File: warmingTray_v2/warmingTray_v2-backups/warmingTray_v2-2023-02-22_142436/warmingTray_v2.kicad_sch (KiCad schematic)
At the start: 37 parts, among them J1 Jack-DC, P1 Power, P2 Analog, P3 Analog, P4 Digital, P5 PWM, P6 PWM, P7 Communication

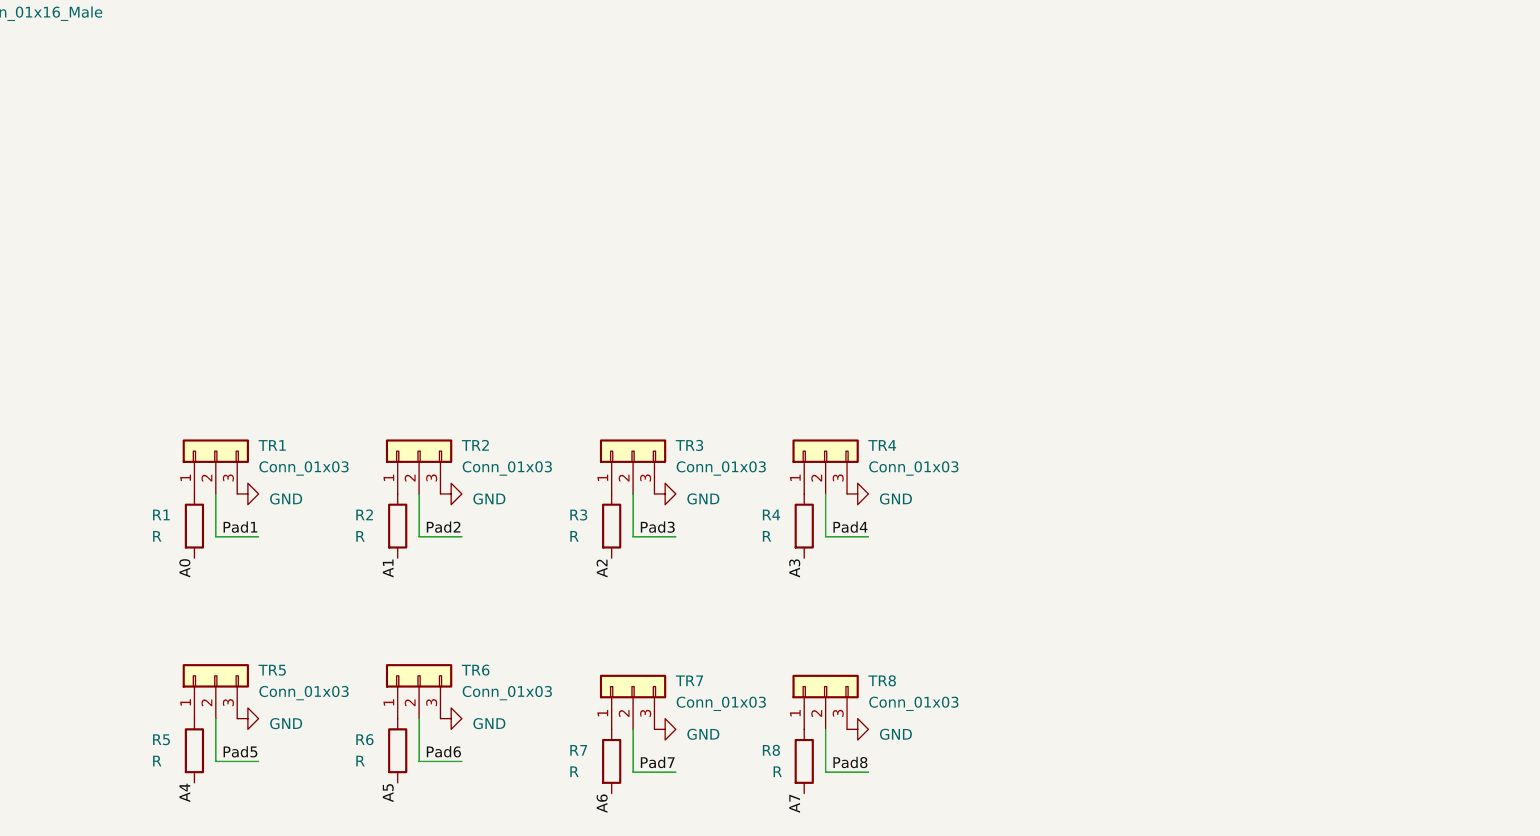
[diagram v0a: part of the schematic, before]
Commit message: Added footprints for transistor pins and surface mount resistors
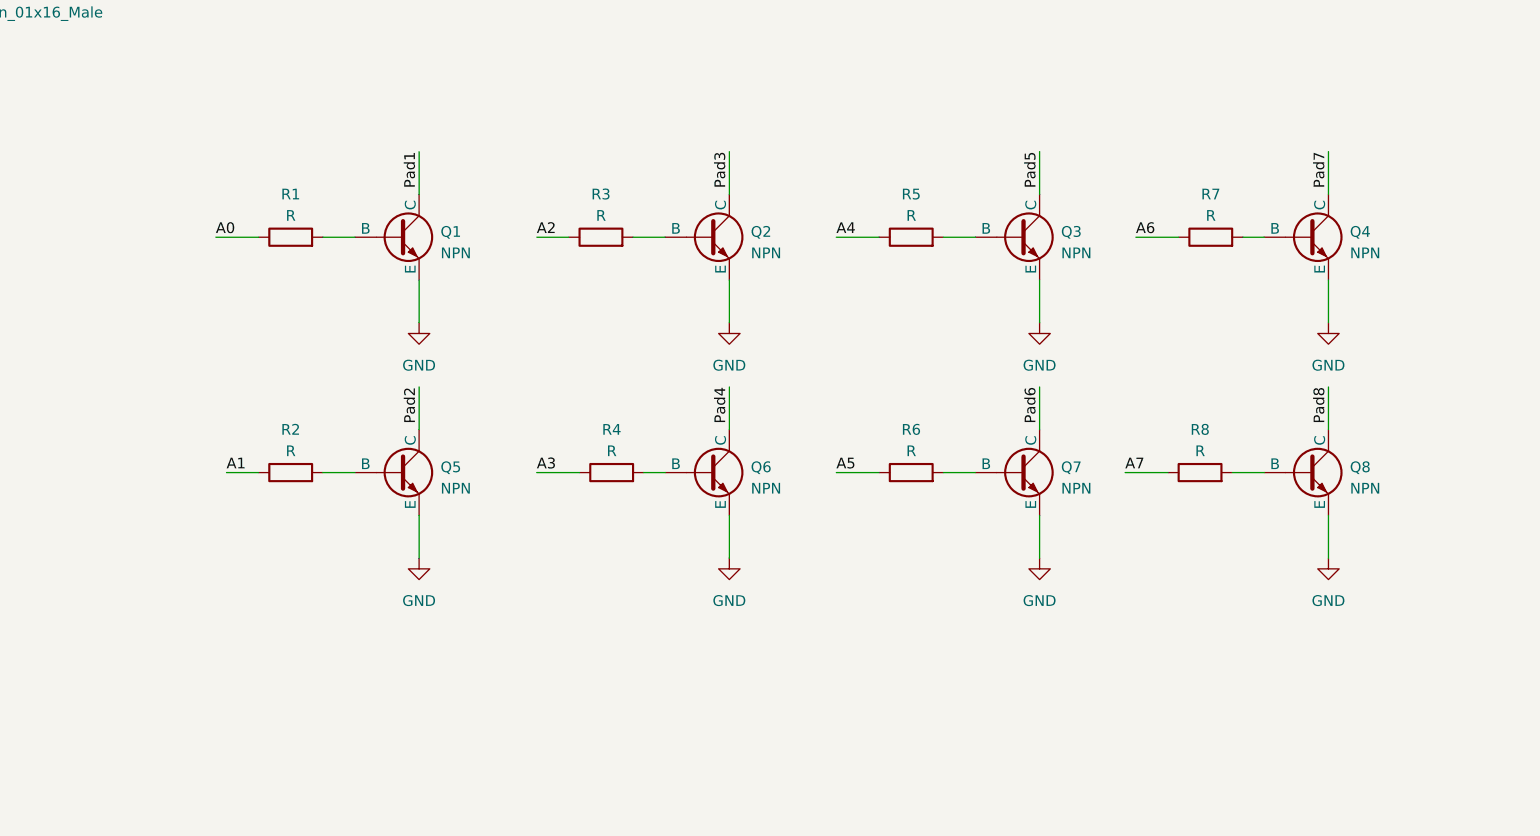
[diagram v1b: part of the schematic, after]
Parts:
- removed TR1, TR2, TR3, TR4, TR5, TR6, TR7, TR8: Conn_01x03, Connector_PinSocket_2.54mm:PinSocket_1x03_P2.54mm_Vertical, symbol Connector_Generic:Conn_01x03
- added Q1, Q2, Q3, Q4, Q5, Q6, Q7, Q8: NPN, symbol Simulation_SPICE:NPN
- R1, R2, R3, R4, R5, R6, R7, R8: footprint footprints:RES_RK73G2A_KOA -> (none)
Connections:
- net A0: now also R1.1; no longer R1.2
- net A1: now also R2.1; no longer R2.2
- net A2: now also R3.1; no longer R3.2
- net A3: now also R4.1; no longer R4.2
- net A4: now also R5.1; no longer R5.2
- net A5: now also R6.1; no longer R6.2
- net A6: now also R7.1; no longer R7.2
- net A7: now also R8.1; no longer R8.2
- net GND: now also Q1.3 (E), Q2.3 (E), Q3.3 (E), Q4.3 (E), Q5.3 (E), Q6.3 (E), Q7.3 (E), Q8.3 (E)
- net Pad1: now also Q1.1 (C)
- net Pad2: now also Q5.1 (C)
- net Pad3: now also Q2.1 (C)
- net Pad4: now also Q6.1 (C)
- net Pad5: now also Q3.1 (C)
- net Pad6: now also Q7.1 (C)
- net Pad7: now also Q4.1 (C)
- net Pad8: now also Q8.1 (C)
- new net: Q4.2 (B), R7.2
- new net: Q5.2 (B), R2.2
- new net: Q6.2 (B), R4.2
- new net: Q1.2 (B), R1.2
- new net: Q8.2 (B), R8.2
- new net: Q2.2 (B), R3.2
- new net: Q7.2 (B), R6.2
- new net: Q3.2 (B), R5.2
